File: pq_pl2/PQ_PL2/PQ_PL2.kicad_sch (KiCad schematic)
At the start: 66 parts, among them J1 SLW-110-01-T-S, J2 SLW-110-01-T-S, J3 SLW-110-01-T-S, J4 SLW-110-01-T-S

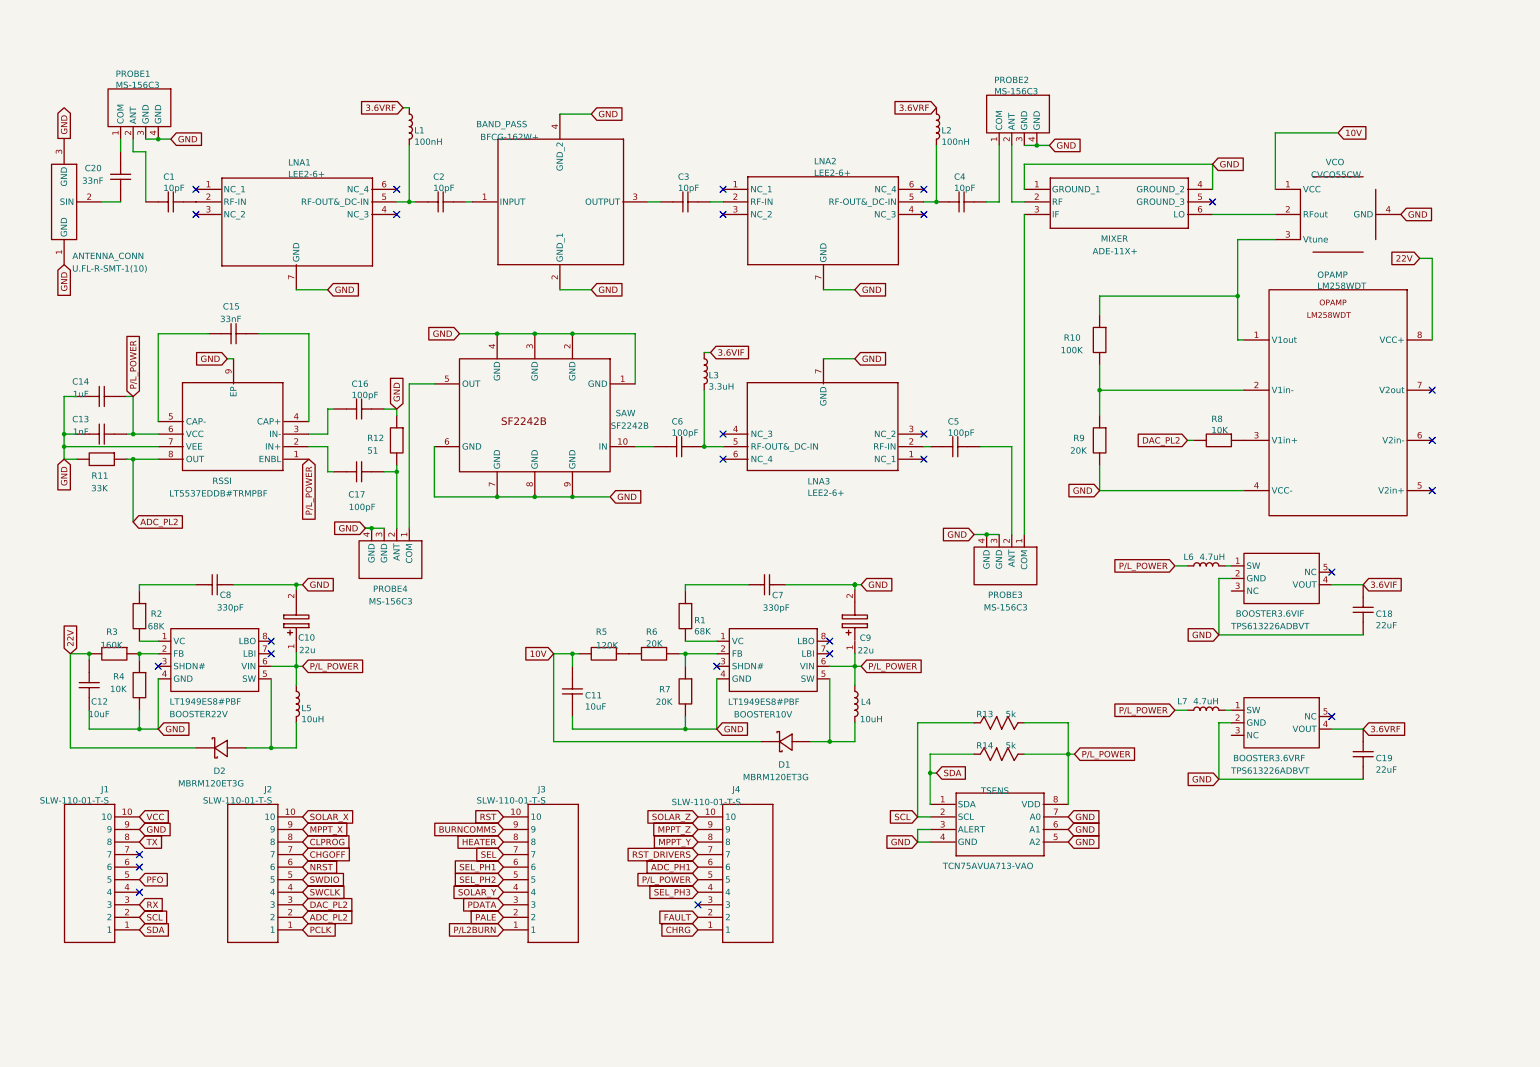
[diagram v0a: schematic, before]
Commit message: Solved old design components&library altium import problems. Pre KiCad7
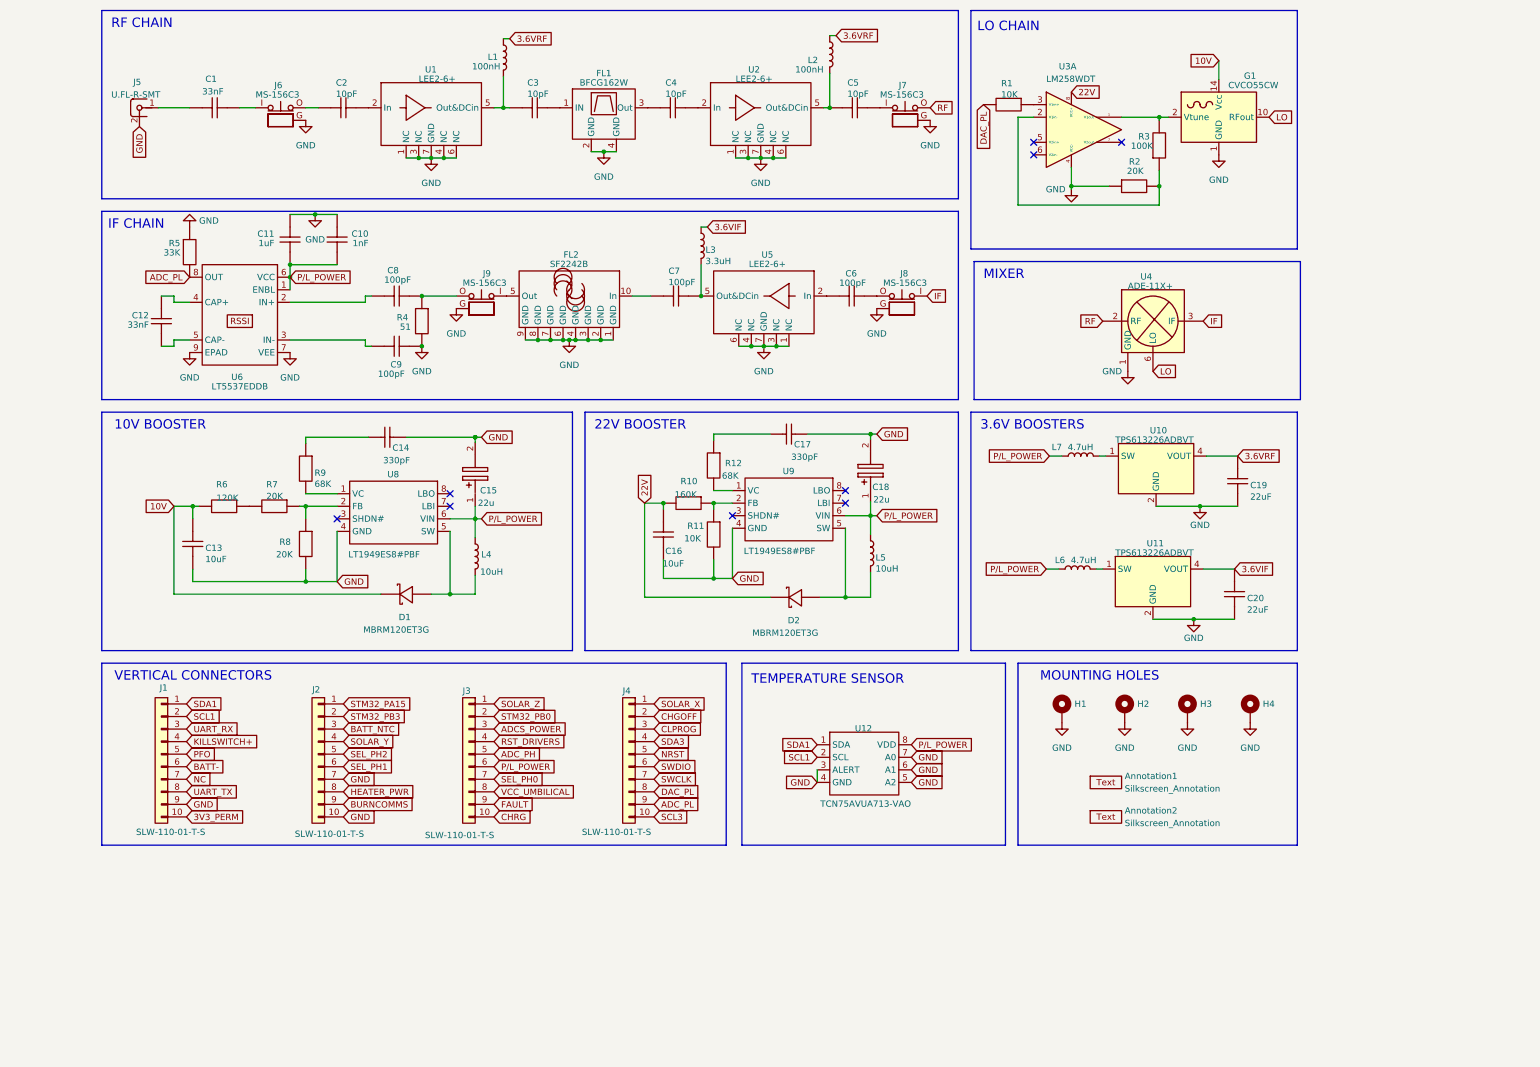
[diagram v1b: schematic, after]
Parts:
- removed BAND_PASS: BFCG-162W+, BFCG162W, symbol L2_PCB-altium-import:0_BFCG-162W+
- removed R13, R14: 5k, R0805, symbol L2_PCB-altium-import:0_5k
- added Annotation1: Silkscreen_Annotation, symbols-nsl:Bridgemaker, symbol symbols-nsl:Silkscreen_Annotation
- added Annotation2: Silkscreen_Annotation, symbols-nsl:GRSS, symbol symbols-nsl:Silkscreen_Annotation
- added FL1: BFCG162W, rf-nsl:GE0805C-3, symbol rf-nsl:BFCG162W
- added H1, H2, H3, H4: MountingHole_Pad, MountingHole:MountingHole_3.2mm_M3_Pad, symbol Mechanical:MountingHole_Pad
- C1: renamed from C20; footprint C0603 -> Capacitor_SMD:C_0603_1608Metric
- C10: renamed from C13; footprint C0603 -> Capacitor_SMD:C_0603_1608Metric
- C11: renamed from C14; footprint C0603 -> Capacitor_SMD:C_0603_1608Metric
- C12: renamed from C15; footprint C0603 -> Capacitor_SMD:C_0603_1608Metric
- C13: renamed from C11; footprint C0603 -> Capacitor_SMD:C_0603_1608Metric
- C14: renamed from C7; footprint C0603 -> Capacitor_SMD:C_0603_1608Metric
- C15: renamed from C9; footprint CAPPM3216X180N -> Capacitor_SMD:C_1206_3216Metric
- C16: renamed from C12; footprint C0603 -> Capacitor_SMD:C_0603_1608Metric
- C17: renamed from C8; footprint C0603 -> Capacitor_SMD:C_0603_1608Metric
- C18: renamed from C10; footprint CAPPM3216X180N -> Capacitor_SMD:C_1206_3216Metric
- C19: footprint C0603 -> Capacitor_SMD:C_0603_1608Metric
- C2: renamed from C1; footprint C0603 -> Capacitor_SMD:C_0603_1608Metric
- C20: renamed from C18; footprint C0603 -> Capacitor_SMD:C_0603_1608Metric
- C3: renamed from C2; footprint C0603 -> Capacitor_SMD:C_0603_1608Metric
- C4: renamed from C3; footprint C0603 -> Capacitor_SMD:C_0603_1608Metric
- C5: renamed from C4; footprint C0603 -> Capacitor_SMD:C_0603_1608Metric
- C6: renamed from C5; footprint C0603 -> Capacitor_SMD:C_0603_1608Metric
- C7: renamed from C6; footprint C0603 -> Capacitor_SMD:C_0603_1608Metric
- C8: renamed from C17; footprint C0603 -> Capacitor_SMD:C_0603_1608Metric
- C9: renamed from C16; footprint C0603 -> Capacitor_SMD:C_0603_1608Metric
- D1, D2: footprint POWERMITE_L2.0-W1.9-LS3.8-RD -> passive-nsl:MBRM120ET3G; symbol L2_PCB-altium-import:0_MBRM120ET3G -> passive-nsl:MBRM120ET3G
- FL2: renamed from SAW; footprint SMP-03-10 5X7 MM -> rf-nsl:SF2242B; symbol L2_PCB-altium-import:3_SF2242B -> rf-nsl:SF2242B
- G1: renamed from VCO; footprint CVCO55CW -> rf-nsl:CVCO55CW; symbol L2_PCB-altium-import:0_CVCO55CW -> Oscillator:CVCO55xx
- J1, J2, J3, J4: footprint SLW-110-01-X-S -> connector-nsl:SLW-110-01; symbol L2_PCB-altium-import:2_SLW-110-01-T-S -> connector-nsl:SLW-110-01
- J5: renamed from ANTENNA_CONN; value U.FL-R-SMT-1(10) -> U.FL-R-SMT; footprint ANT-SMD_UFL-R-SMT-1-10 -> connector-nsl:C.FL-R-SMT-1(90); symbol L2_PCB-altium-import:1_U.FL-R-SMT-1(10) -> connector-nsl:connector-coax
- J6: renamed from PROBE1; footprint IPEX-SMD_MS-156C3 -> connector-nsl:CoaxialSwitch_Hirose_MS-156C3_Horizontal; symbol L2_PCB-altium-import:1_MS-156C3 -> connector-nsl:MS-156C
- J7: renamed from PROBE2; footprint IPEX-SMD_MS-156C3 -> connector-nsl:CoaxialSwitch_Hirose_MS-156C3_Horizontal; symbol L2_PCB-altium-import:1_MS-156C3 -> connector-nsl:MS-156C
- J8: renamed from PROBE3; footprint IPEX-SMD_MS-156C3 -> connector-nsl:CoaxialSwitch_Hirose_MS-156C3_Horizontal; symbol L2_PCB-altium-import:3_MS-156C3 -> connector-nsl:MS-156C
- J9: renamed from PROBE4; footprint IPEX-SMD_MS-156C3 -> connector-nsl:CoaxialSwitch_Hirose_MS-156C3_Horizontal; symbol L2_PCB-altium-import:3_MS-156C3 -> connector-nsl:MS-156C
- L1, L2: footprint L0402 -> Inductor_SMD:L_0603_1608Metric
- L3, L4, L5: footprint L0603 -> Inductor_SMD:L_0603_1608Metric
- L6, L7: footprint L0805 -> Inductor_SMD:L_0603_1608Metric
- R1: renamed from R8; footprint R0603 -> Resistor_SMD:R_0603_1608Metric
- R10: renamed from R3; footprint R0603 -> Resistor_SMD:R_0603_1608Metric
- R11: renamed from R4; footprint R0603 -> Resistor_SMD:R_0603_1608Metric
- R12: renamed from R2; footprint R0603 -> Resistor_SMD:R_0603_1608Metric
- R2: renamed from R9; footprint R0603 -> Resistor_SMD:R_0603_1608Metric
- R3: renamed from R10; footprint R0603 -> Resistor_SMD:R_0603_1608Metric
- R4: renamed from R12; footprint R0603 -> Resistor_SMD:R_0603_1608Metric
- R5: renamed from R11; footprint R0603 -> Resistor_SMD:R_0603_1608Metric
- R6: renamed from R5; footprint R0603 -> Resistor_SMD:R_0603_1608Metric
- R7: renamed from R6; footprint R0603 -> Resistor_SMD:R_0603_1608Metric
- R8: renamed from R7; footprint R0603 -> Resistor_SMD:R_0603_1608Metric
- R9: renamed from R1; footprint R0603 -> Resistor_SMD:R_0603_1608Metric
- U1: renamed from LNA1; footprint SON65P200X200X105-7N -> Package_SON:WSON-6-1EP_2x2mm_P0.65mm_EP1x1.6mm; symbol L2_PCB-altium-import:0_LEE2-6+ -> rf-nsl:LEE2-6+
- U10: renamed from BOOSTER3.6VRF; footprint SOT-23-5_L2.9-W1.6-P0.95-LS2.8-BR -> Package_TO_SOT_SMD:SOT-23-5; symbol L2_PCB-altium-import:0_TPS613226ADBVT -> Regulator_Switching:TPS613226ADBV
- U11: renamed from BOOSTER3.6VIF; footprint SOT-23-5_L2.9-W1.6-P0.95-LS2.8-BR -> Package_TO_SOT_SMD:SOT-23-5; symbol L2_PCB-altium-import:0_TPS613226ADBVT -> Regulator_Switching:TPS613226ADBV
- U12: renamed from TSENS; footprint SOP65P490X110-8N -> Package_SO:SOP-8_3.9x4.9mm_P1.27mm; symbol L2_PCB-altium-import:0_TCN75AVUA713-VAO -> SP_ICs:TCN75AVUA713
- U2: renamed from LNA2; footprint SON65P200X200X105-7N -> Package_SON:WSON-6-1EP_2x2mm_P0.65mm_EP1x1.6mm; symbol L2_PCB-altium-import:0_LEE2-6+ -> rf-nsl:LEE2-6+
- U3: renamed from OPAMP; footprint SO8 -> Package_SO:SO-8_3.9x4.9mm_P1.27mm; symbol L2_PCB-altium-import:0_LM258WDT -> power-nsl:LM258
- U4: renamed from MIXER; footprint SOTFL254P691X284-6N -> rf-nsl:SOTFL254P691X284-6N; symbol L2_PCB-altium-import:0_ADE-11X+ -> rf-nsl:ADE-11X
- U5: renamed from LNA3; footprint SON65P200X200X105-7N -> Package_SON:WSON-6-1EP_2x2mm_P0.65mm_EP1x1.6mm; symbol L2_PCB-altium-import:2_LEE2-6+ -> rf-nsl:LEE2-6+
- U6: renamed from RSSI; value LT5537EDDB#TRMPBF -> LT5537EDDB; footprint SON50P200X300X80-9N -> Package_DFN_QFN:DFN-8-1EP_2x3mm_P0.5mm_EP0.56x2.15mm; symbol L2_PCB-altium-import:2_LT5537EDDB#TRMPBF -> rf-nsl:LT5537
- U8: renamed from BOOSTER10V; footprint SO-8_L4.9-W3.9-P1.27-LS5.9-BL -> Package_SO:SO-8_3.9x4.9mm_P1.27mm; symbol L2_PCB-altium-import:0_LT1949ES8#PBF -> power-nsl:LT1949
- U9: renamed from BOOSTER22V; footprint SO-8_L4.9-W3.9-P1.27-LS5.9-BL -> Package_SO:SO-8_3.9x4.9mm_P1.27mm; symbol L2_PCB-altium-import:0_LT1949ES8#PBF -> power-nsl:LT1949
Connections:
- net ADC_PH1 is gone; now on net SWDIO: J4.6
- net MPPT_X is gone; now on net BURNCOMMS: J2.9
- net P/L2BURN is gone; now on net SOLAR_Z: J3.1
- net RST is gone; now on net CHRG: J3.10
- net 10V: now also G1.14 (Vcc); no longer G1.1 (VCC)
- net BURNCOMMS: no longer J3.9
- net CHGOFF: now also J4.2; no longer J2.7
- net CHRG: no longer J4.1
- net CLPROG: now also J4.3; no longer J2.8
- net FAULT: now also J3.9; no longer J4.2
- net GND: now also C10.1, C11.1, G1.1 (GND), G1.11 (GND), G1.12 (GND), G1.13 (GND), G1.15 (GND), G1.16 (GND), G1.3 (GND), G1.5 (GND), G1.6 (GND), G1.7 (GND), G1.8 (GND), G1.9 (GND), J2.10, J2.7, J5.2, J6.G, J7.G, J8.G, J9.G, R2.1, R4.2, R5.1, U1.1 (NC), U1.3 (NC), U1.4 (NC), U1.6 (NC), U2.1 (NC), U2.3 (NC), U2.4 (NC), U2.6 (NC), U4.5 (GND), U5.1 (NC), U5.3 (NC), U5.4 (NC), U5.6 (NC), FL1.2 (GND), FL1.4 (GND), H1.1, H2.1, H3.1, H4.1; no longer C10.2, C11.2, J5.1 (GND), J6.3 (GND), J6.4 (GND), J7.3 (GND), J7.4 (GND), J8.3 (GND), J8.4 (GND), J9.3 (GND), J9.4 (GND), R2.2, R4.1, R5.2
- net NRST: now also J4.5; no longer J2.6
- net P/L_POWER: now also C10.2, C11.2, J3.6; no longer C10.1, C11.1, J4.5
- net RST_DRIVERS: now also J3.4; no longer J4.7
- net SEL_PH1: now also J2.6; no longer J3.6
- net SEL_PH2: now also J2.5; no longer J3.5
- net SOLAR_X: now also J4.1; no longer J2.10
- net SOLAR_Y: now also J2.4; no longer J3.4
- net SOLAR_Z: no longer J4.10
- net SWCLK: now also J4.7; no longer J2.4
- net SWDIO: no longer J2.5
- net KILLSWITCH+: now reaches J1.4
- net BATT-: now reaches J1.6
- net NC: now reaches J1.7
- net at C4.1: now also FL1.3 (Out)
- net at FL2.5 (Out): now also J9.I; no longer J9.1 (COM)
- net at C1.1: now also J6.I; no longer J6.1 (COM)
- net at C1.2: now also J5.1; no longer J5.2 (SIN)
- net at C2.1: now also J6.O; no longer J6.2 (ANT)
- net at C5.2: now also J7.I; no longer J7.1 (COM)
- net RF: now reaches U4.2 (RF)
- net RF: now also J7.O; no longer J7.2 (ANT)
- net at C6.2: now also J8.O; no longer J8.2 (ANT)
- net IF: now reaches U4.3 (IF)
- net IF: now also J8.I; no longer J8.1 (COM)
- net at G1.2 (Vtune): now also R3.1, U3.1 (V1out); no longer U4.6 (LO)
- net at C3.2: now also FL1.1 (IN)
- removed net ADC_PL2: J2.2, R5.1, U6.8 (OUT)
- net DAC_PL2 renamed BATT_NTC
- net BATT_NTC: no longer R1.2
- net HEATER renamed VCC_UMBILICAL
- net MPPT_Y renamed DAC_PL
- net DAC_PL: now also R1.2
- net MPPT_Z renamed ADC_PL
- net ADC_PL: now also R5.2, U6.8 (OUT)
- net PALE renamed STM32_PB0
- net PCLK renamed STM32_PA15
- net PDATA renamed ADCS_POWER
- net RX renamed UART_RX
- net SCL renamed SCL1
- net SDA renamed SDA1
- net SEL renamed SEL_PH0
- net SEL_PH3 renamed SDA3
- net TX renamed UART_TX
- net VCC renamed 3V3_PERM
- new net: C8.2, J9.O, R4.1
- new net: R2.2, R3.2, U3.2 (V1in-)
- new net ADC_PH: J3.5
- new net HEATER_PWR: J2.8
- new net LO: G1.10 (RFout), U4.6 (LO)
- new net SCL3: J4.10
- new net STM32_PB3: J2.2
- no-connect marks 28 -> 9
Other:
- note added: "10V BOOSTER"
- note added: "22V BOOSTER"
- note added: "3.6V BOOSTERS"
- note added: "IF CHAIN"
- note added: "LO CHAIN"
- note added: "MIXER"
- note added: "MOUNTING HOLES"
- note added: "RF CHAIN"
- note added: "TEMPERATURE SENSOR"
- note added: "VERTICAL CONNECTORS"
- moved on the sheet: C1, C10, C11, C12, C13, C14, C15, C16, C17, C18, C19, C2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

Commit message: Full Kicad7 transition, library improvement and adaptation, correct footprints and 3D models added
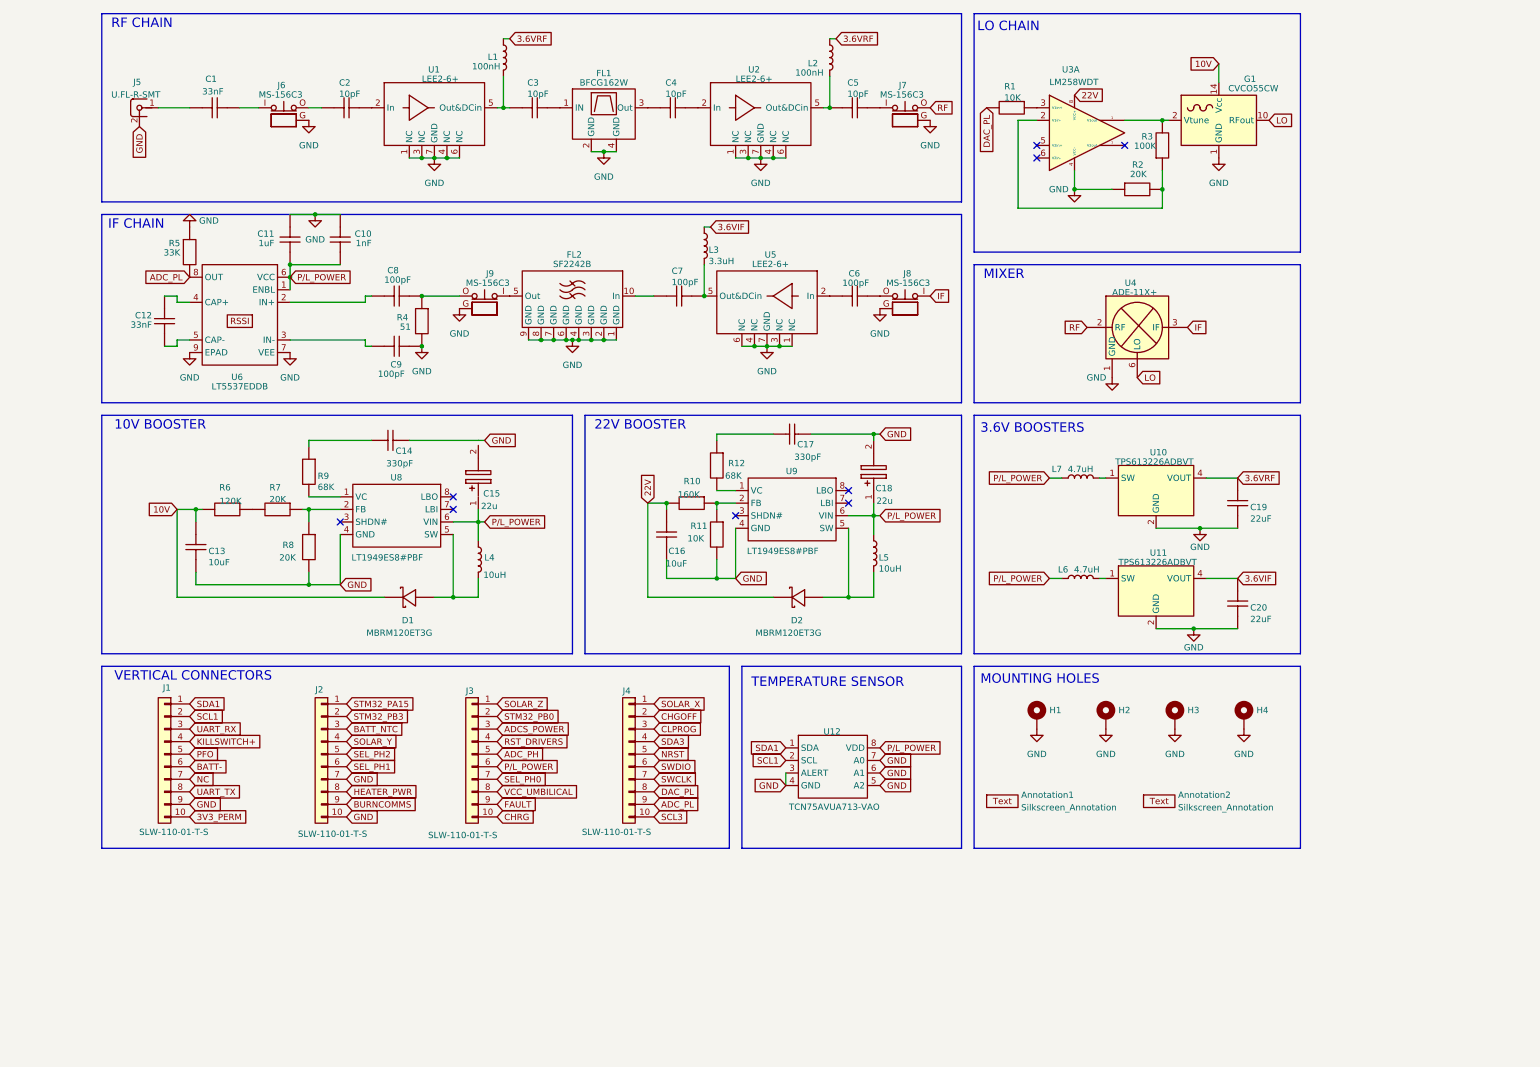
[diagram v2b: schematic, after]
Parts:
- Annotation1: footprint symbols-nsl:Bridgemaker -> -nsl_symbols:Bridgemaker
- Annotation2: footprint symbols-nsl:GRSS -> -nsl_symbols:GRSS
- D1, D2: footprint passive-nsl:MBRM120ET3G -> -nsl_passive:MBRM120ET3G
- FL1: footprint rf-nsl:GE0805C-3 -> -nsl_rf:GE0805C-3
- FL2: footprint rf-nsl:SF2242B -> -nsl_rf:SF2242B
- G1: footprint rf-nsl:CVCO55CW -> RF_Mini-Circuits:Mini-Circuits_CK605_LandPatternPL-012
- J1, J2, J3, J4: footprint connector-nsl:SLW-110-01 -> -nsl_connector:BBL-110-Y-X
- J5: footprint connector-nsl:C.FL-R-SMT-1(90) -> -nsl_connector:C.FL-R-SMT-1(90)
- J6, J7, J8, J9: footprint connector-nsl:CoaxialSwitch_Hirose_MS-156C3_Horizontal -> -nsl_connector:CoaxialSwitch_Hirose_MS-156C3_Horizontal
- U4: footprint rf-nsl:SOTFL254P691X284-6N -> -nsl_rf:SOTFL254P691X284-6N
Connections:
- net GND: no longer C18.2 (-)
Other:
- moved on the sheet: Annotation1, Annotation2, C10, C12, C13, C14, C15, C16, C17, C18, C19, C2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
